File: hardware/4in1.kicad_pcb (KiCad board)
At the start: 6 copper layers, 41.6 x 42.5 mm, 217 parts, among them J1 SM08B-SRSS-TB, Q1 SP40N01GHNK, Q10 SP40N01GHNK, Q11 SP40N01GHNK, Q12 SP40N01GHNK, Q13 SP40N01GHNK, Q14 SP40N01GHNK, Q15 SP40N01GHNK, Q16 SP40N01GHNK, Q17 SP40N01GHNK, Q18 SP40N01GHNK, Q19 SP40N01GHNK, Q2 SP40N01GHNK, Q20 SP40N01GHNK, Q21 SP40N01GHNK, Q22 SP40N01GHNK, Q23 SP40N01GHNK, Q24 SP40N01GHNK, Q3 SP40N01GHNK, Q4 SP40N01GHNK, Q5 SP40N01GHNK, Q6 SP40N01GHNK, Q7 SP40N01GHNK, Q8 SP40N01GHNK, Q9 SP40N01GHNK, U10 NSG2065Q, U12 INA186A3IDCKR, U13 LMR54406DBVR, U14 FTC160808S4R7MBCA, U15 TLV76733DRVR, U2 AT32F421G8U7, U4 NSG2065Q, U5 AT32F421G8U7, U6 NSG2065Q, U7 AT32F421G8U7, U8 NSG2065Q, U9 AT32F421G8U7

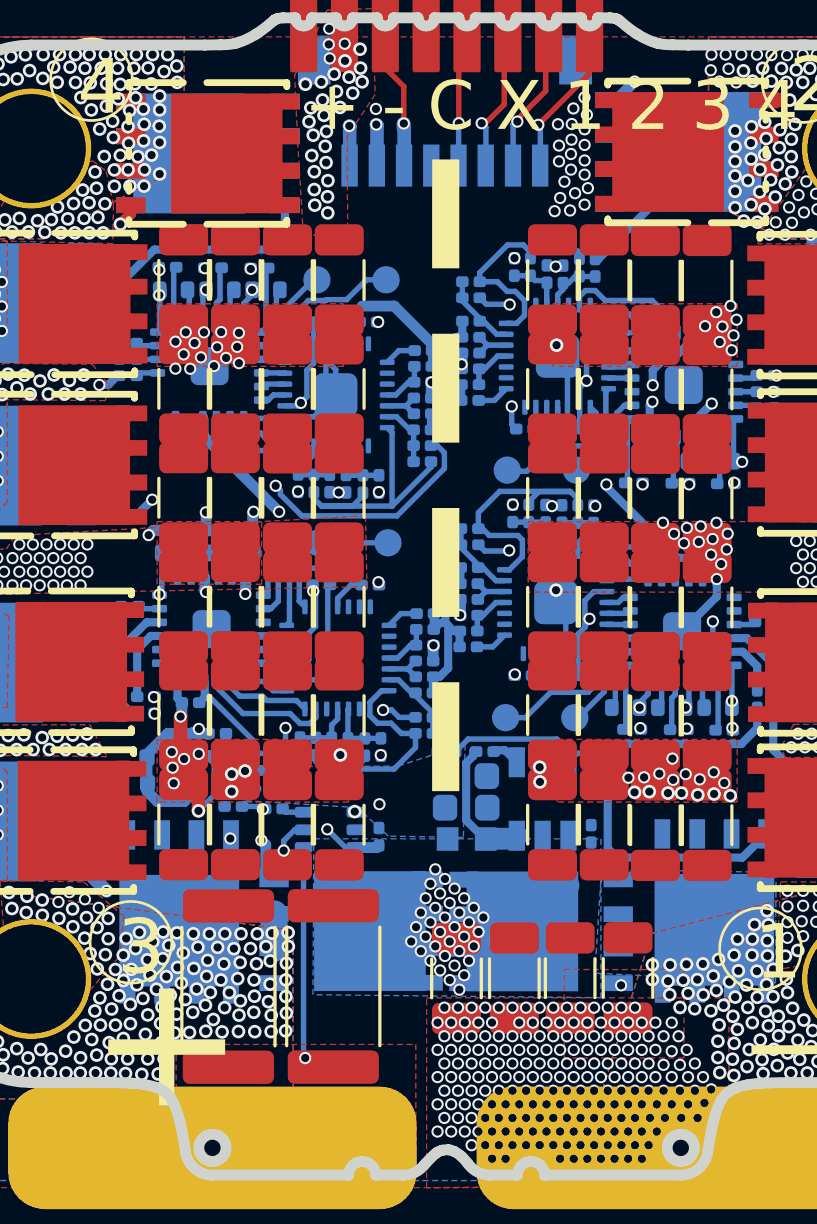
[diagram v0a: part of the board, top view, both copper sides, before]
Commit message: CSA input filter: starve the high-side feedthrough before the amplifier
/CURR was garbage below full throttle, measured 2026-08-21 on the 20x20
sibling: bus common-mode at 24-54 kHz rectifies in the INA186 front end,
whose CMRR is ~80 dB there against an 8 mV full-scale signal.

R89/R90 1k (C270365) in each sense leg, C40/C41 100n 50V (C307331) to
ground, C42 1u (C7500381) across the amplifier inputs. Worst-case SPICE
(1% R, 10% C mismatch, 10 Vpp CM at 50 kHz): common-mode at the pins
drops 300x, converted differential ripple 2.8 mVpp, DC gain error
-0.08 percent. C42 does the load-bearing work: without it the C40/C41
mismatch converts CM to 59 mVpp of differential, 7x full scale. Values
hold with the CM caps derated to 30 percent at full bus bias because
C42 sits at zero bias. Per TI SBOS318B section 8.1.3, input filtering
costs nothing at the INA186's pA bias currents.

Gates: ERC errors all pre-existing benign pin-type classes, new
subcircuit connectivity verified against the netlist; DRC 0 errors,
parity at the documented 89 board-only items, copper sliver pre-exists
at HEAD and HEAD's connection_width warning is gone; model preflight
0 blocking.

Acceptance test: ESC-04 mid-throttle i_a vs clamp sweep on this rev.

Co-Authored-By: Claude Fable 5 <noreply@anthropic.com>
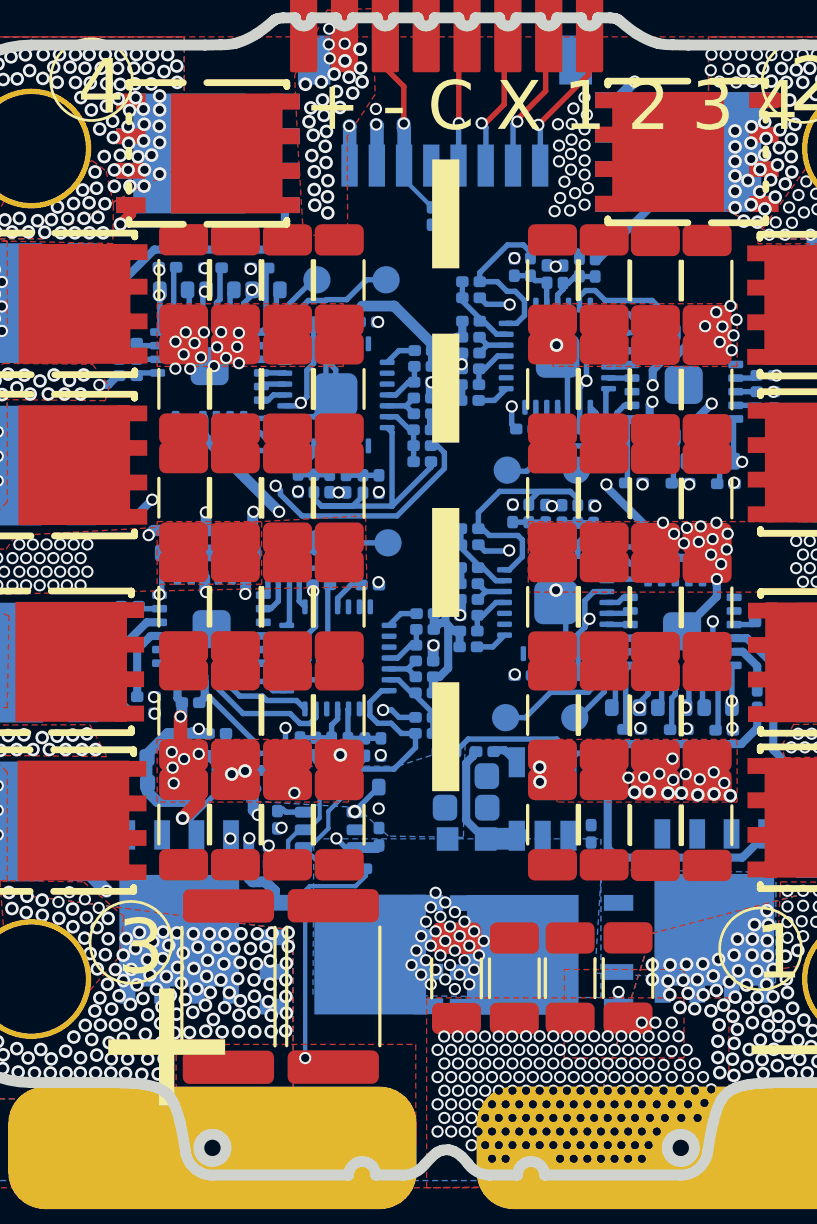
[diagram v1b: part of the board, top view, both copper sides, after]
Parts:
- added C40: 100nF, Capacitor_SMD:C_0402_WIDE, B.Cu at (70.8, 55.6)
- added C41: 100nF, Capacitor_SMD:C_0402_WIDE, B.Cu at (72.6, 55.5)
- added C42: 1uF, 4in1ESC-30x30:C_0402_1005Metric, B.Cu at (70.7, 58.6)
- added R89: 1k, Capacitor_SMD:C_0201_0603Metric, B.Cu at (69.1, 58.0)
- added R90: 1k, Capacitor_SMD:C_0201_0603Metric, B.Cu at (72.3, 58.5)
- moved C94 22.9 mm to (75.1, 34.6), turned to -90 degrees
- moved Q18 0.86 mm to (72.1, 61.7)
- moved Q1 0.86 mm to (79.1, 61.7)
- moved R73 0.42 mm to (69.4, 56.8), turned to 90 degrees
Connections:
- U12 pad 4: /CSA+ -> Net-(U12-+IN)
- U12 pad 5: +BATT -> Net-(U12--IN)
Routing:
- net +10V: track 49.7 -> 61.2 mm, vias 4 -> 5
- net Net-(U12--IN): track 0.00 -> 5.09 mm
- net Net-(U12-+IN): track 0.00 -> 5.07 mm
- net +BATT: track 6.66 -> 3.11 mm, vias 38 -> 34
- net GND: track 61.1 -> 63.9 mm, vias 555 -> 526
- net Net-(Q18-G): track 17.0 -> 19.2 mm
- net /CURR: track 33.6 -> 35.7 mm
- net /ESC3/MotorC: track 26.8 -> 25.5 mm
- net /CSA+: track 7.75 -> 8.86 mm
- net Net-(Q1-G): track 12.2 -> 12.9 mm
- net +3V3: track 88.1 -> 87.5 mm
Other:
- board text added: "4 3 2 1 C - +"
- board text removed: "4 3 2 1 X C - +"
